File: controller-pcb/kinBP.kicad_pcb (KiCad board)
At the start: 2 copper layers, 100 x 86.5 mm, 30 parts, among them J1 LEFT_TOP, J10 LEFT_THUMB, J11 RIGHT_THUMB, J12 RIGHT_THUMB, J13 LEFT_THUMB, J2 LEFT_TOP, J3 RIGHT_TOP, J4 RIGHT_TOP, J5 RIGHT_KEYWELL, J6 LEFT_KEYWELL, J7 LEFT_THUMB, J8 RIGHT_THUMB, J9 Conn_02x08_Odd_Even, U1 weact_STM32F4x1

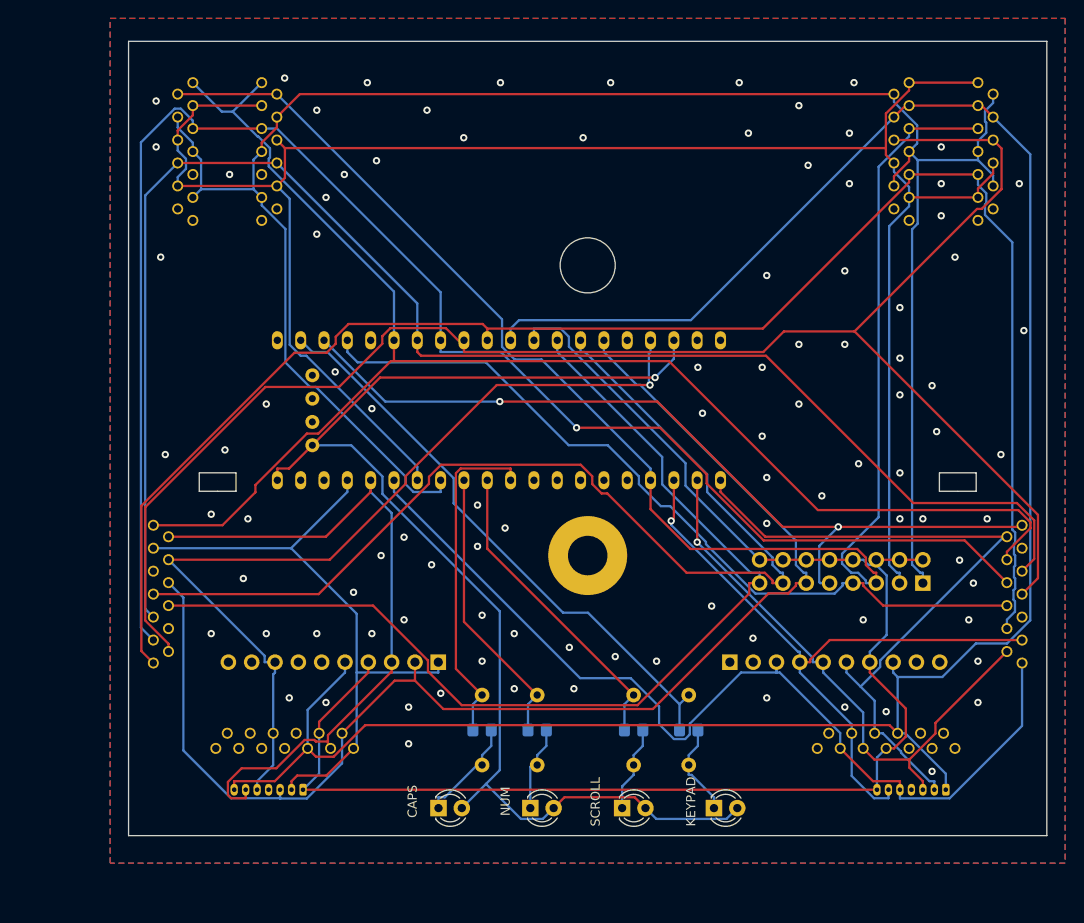
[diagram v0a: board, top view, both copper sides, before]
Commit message: River's modified version. Added piezo sounder. Rerouted. Split extra switch header.
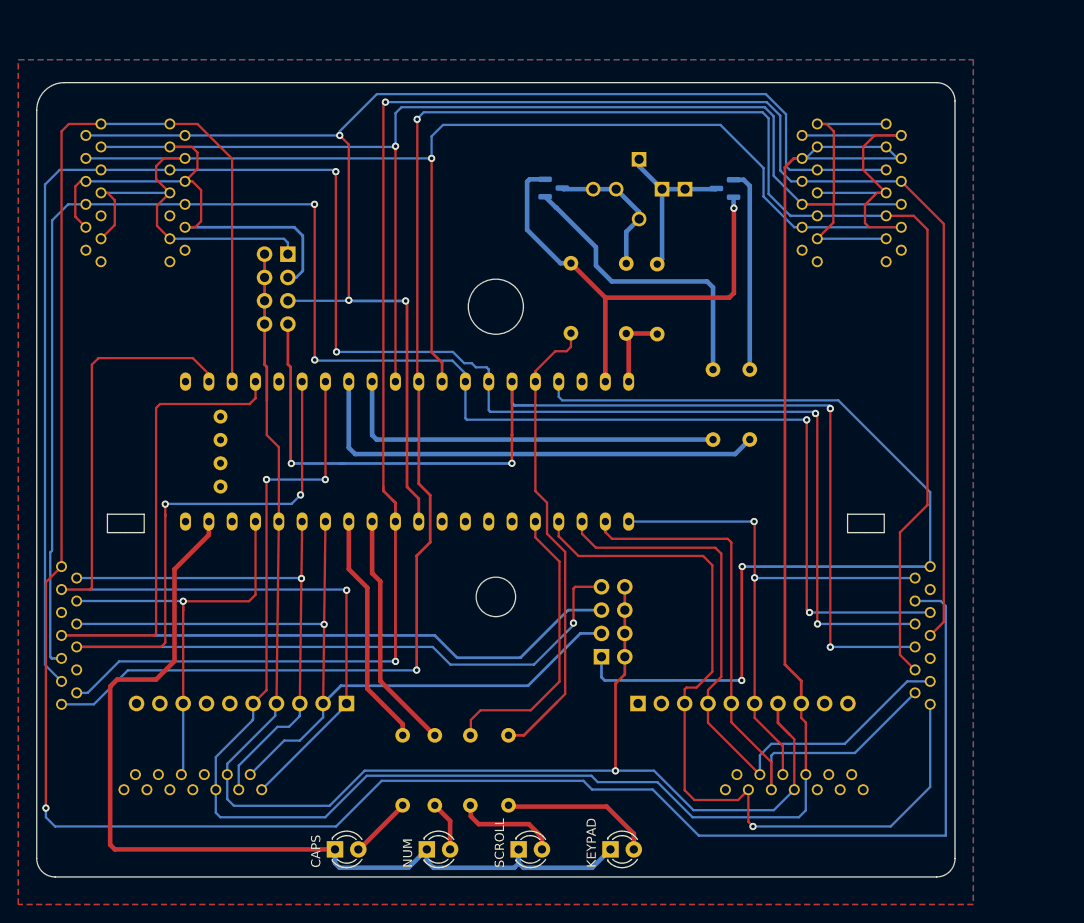
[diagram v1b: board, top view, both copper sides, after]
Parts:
- removed G***: LOGO, logo:qmk-small
- removed G1: LOGO, logo:q64logo
- removed J12: RIGHT_THUMB, Connector_Molex:Molex_PicoBlade_53048-0710_1x07_P1.25mm_Horizontal
- removed J13: LEFT_THUMB, Connector_Molex:Molex_PicoBlade_53048-0710_1x07_P1.25mm_Horizontal
- added J14: Conn_02x04_Odd_Even, Connector_PinHeader_2.54mm:PinHeader_2x04_P2.54mm_Vertical, B.Cu at (109.3, 73.7)
- added LS1: Speaker_Crystal, river:Piezos_12mm, B.Cu at (147.6, 66.6)
- added Q1: MMBT3904, Package_TO_SOT_SMD:SOT-23, B.Cu at (156.9, 66.5)
- added Q2: MMBT3904, Package_TO_SOT_SMD:SOT-23, B.Cu at (138.3, 66.5)
- added R9: R, Resistor_THT:R_Axial_DIN0207_L6.3mm_D2.5mm_P7.62mm_Horizontal, B.Cu at (146.2, 74.7)
- H1: value mounting pad -> hole; footprint MountingHole:MountingHole_4.3mm_M4_Pad -> MountingHole:MountingHole_4.3mm_M4
- H2: value mounting pad -> hole
- J9: value Conn_02x08_Odd_Even -> Conn_02x04_Odd_Even; footprint Connector_PinHeader_2.54mm:PinHeader_2x08_P2.54mm_Vertical -> Connector_PinHeader_2.54mm:PinHeader_2x04_P2.54mm_Vertical
- LED1, LED2, LED3, LED4: footprint LED_THT:LED_D3.0mm -> keyboards:LED_D3.0mm_centered
- R1: value 1k -> 100k; footprint Resistor_SMD:R_0805_2012Metric_Pad1.20x1.40mm_HandSolder -> Resistor_THT:R_Axial_DIN0207_L6.3mm_D2.5mm_P7.62mm_Horizontal
- R2, R3, R4: value 1k -> R; footprint Resistor_SMD:R_0805_2012Metric_Pad1.20x1.40mm_HandSolder -> Resistor_THT:R_Axial_DIN0207_L6.3mm_D2.5mm_P7.62mm_Horizontal
- moved R4 54.2 mm to (149.6, 74.8), turned to -90 degrees
- moved R1 45.1 mm to (140.2, 82.3), turned to 90 degrees
- moved R3 37.0 mm to (155.7, 93.9), turned to 90 degrees
- moved J9 35.9 mm to (143.5, 117.5), turned to 0 degrees
- moved R2 34.1 mm to (159.7, 93.9), turned to 90 degrees
- moved R5 23.0 mm to (133.4, 133.7), turned to 90 degrees
- moved R6 21.5 mm to (129.2, 133.7), turned to 90 degrees
- moved R7 16.4 mm to (125.3, 133.7), turned to 90 degrees
- moved R8 14.8 mm to (121.8, 133.7), turned to 90 degrees
- moved H1 11.0 mm to (132.0, 111.0)
- moved H2 11.0 mm to (132.0, 79.4)
- moved J1 11.0 mm to (96.5, 67.0)
- moved J10 11.0 mm to (99.0, 132.0)
- moved J11 11.0 mm to (164.5, 132.0)
- moved J2 11.0 mm to (89.0, 67.0)
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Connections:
- J7 pad 9: unconnected-(J7-Pad9) -> GND
- J8 pad 9: unconnected-(J8-Pad9) -> GND
- J9 pad 1: ROW_E -> ROW_A
- J9 pad 3: ROW_D -> ROW_2
- J9 pad 5: ROW_C -> ROW_1
- J9 pad 7: ROW_B -> ROW_0
- LED1 pad 1: LED_KPD_R -> GND
- LED1 pad 2: /3V3 -> Net-(LED1-A)
- LED2 pad 1: LED_SCRL_R -> GND
- LED2 pad 2: /3V3 -> Net-(LED2-A)
- LED3 pad 1: LED_NUM_R -> GND
- LED3 pad 2: /3V3 -> Net-(LED3-A)
- LED4 pad 1: LED_CAPS_R -> GND
- LED4 pad 2: /3V3 -> Net-(LED4-A)
- R1 pad 2: LED_KPD_R -> GND
- R2 pad 1: LED_SCRL -> PIEZO_A
- R2 pad 2: LED_SCRL_R -> Net-(Q1-B)
- R3 pad 1: LED_NUM -> PIEZO_B
- R3 pad 2: LED_NUM_R -> Net-(Q2-B)
- R4 pad 1: LED_CAPS -> Net-(Q1-C)
- R4 pad 2: LED_CAPS_R -> +5V
- R5 pad 1: LED_KPD -> Net-(LED1-A)
- R5 pad 2: LED_KPD_R -> LED_KPD
- R6 pad 1: LED_SCRL -> Net-(LED2-A)
- R6 pad 2: LED_SCRL_R -> LED_SCRL
- R7 pad 1: LED_NUM -> Net-(LED3-A)
- R7 pad 2: LED_NUM_R -> LED_NUM
- R8 pad 1: LED_CAPS -> Net-(LED4-A)
- R8 pad 2: LED_CAPS_R -> LED_CAPS
- U1 pad 10: LED_CAPS -> ROW_C
- U1 pad 11: LED_SCRL -> COL_3
- U1 pad 13: ROW_E -> LED_CAPS
- U1 pad 14: ROW_D -> ROW_2
- U1 pad 15: ROW_6 -> ROW_5
- U1 pad 16: ROW_5 -> COL_6
- U1 pad 17: ROW_4 -> ROW_3
- U1 pad 20: /3V3 -> +3V3
- U1 pad 22: LED_KPD -> ROW_4
- U1 pad 23: ROW_A -> COL_0
- U1 pad 24: ROW_B -> ROW_1
- U1 pad 26: COL_0 -> ROW_0
- U1 pad 27: COL_1 -> COL_5
- U1 pad 28: COL_2 -> PIEZO_A
- U1 pad 29: COL_3 -> PIEZO_B
- U1 pad 30: COL_4 -> ROW_D
- U1 pad 31: COL_5 -> COL_4
- U1 pad 32: COL_6 -> ROW_E
- U1 pad 33: ROW_0 -> COL_1
- U1 pad 34: ROW_1 -> COL_2
- U1 pad 35: ROW_2 -> ROW_B
- U1 pad 36: unconnected-(U1-Pad36) -> LED_KPD
- U1 pad 37: ROW_3 -> ROW_A
- U1 pad 38: /3V3 -> unconnected-(U1-3V3-Pad38)
- U1 pad 4: ROW_C -> ROW_6
- U1 pad 40: unconnected-(U1-Pad40) -> +5V
- U1 pad 41: /3V3 -> unconnected-(U1-3V3-Pad41)
- U1 pad 44: GND -> unconnected-(U1-GND-Pad44)
- U1 pad 5: unconnected-(U1-Pad5) -> LED_SCRL
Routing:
- net GND: track 0.00 -> 157.9 mm, vias 97 -> 1
- net /3V3: track 135.0 -> 0.00 mm, vias 1 -> 0
- net COL_0: track 160.5 -> 251.7 mm, vias 0 -> 1
- net PIEZO_A: track 0.00 -> 51.8 mm
- net ROW_3: track 97.1 -> 46.9 mm
- net ROW_2: track 142.2 -> 92.3 mm, vias 0 -> 1
- net PIEZO_B: track 0.00 -> 43.1 mm
- net COL_4: track 178.3 -> 217.0 mm, vias 0 -> 2
- net ROW_B: track 86.5 -> 120.7 mm, vias 0 -> 4
- net Net-(Q2-B): track 0.00 -> 32.5 mm
- net COL_3: track 182.1 -> 213.3 mm, vias 0 -> 2
- net ROW_4: track 69.0 -> 97.9 mm, vias 0 -> 1
- net COL_5: track 242.5 -> 219.2 mm, vias 0 -> 2
- net Net-(Q1-B): track 0.00 -> 22.0 mm
- net COL_2: track 176.9 -> 198.2 mm, vias 1 -> 4
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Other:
- outline, holes or cut-outs redrawn
- board text added: "Kinesis Black Pill V0.1 https://river.cat/t/kinbp"
- board text removed: "Col 6"
- board text removed: "KinBP v1.21"
- board text removed: "Open Hardware: CC-BY-SA"
- board text removed: "Rows E D C B A 2 1 0"
- board text removed: "github.com/DmNosachev/kinbp"
- board text removed: "pads"
- board text removed: "↑"

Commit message: V0.1 as manufactured
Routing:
- net ROW_6: track 88.2 -> 78.3 mm
- net ROW_7: track 68.4 -> 60.4 mm
- net ROW_8: track 66.3 -> 60.0 mm
- net COL_0: track 251.7 -> 245.9 mm
- net ROW_E: track 202.5 -> 198.8 mm
- net COL_5: track 219.2 -> 216.6 mm
- net ROW_D: track 207.9 -> 205.3 mm
- net COL_4: track 217.0 -> 214.9 mm
- net GND: track 157.9 -> 155.8 mm, vias 1 -> 220
- net COL_6: track 159.0 -> 156.9 mm
- net LED_KPD: track 51.0 -> 48.9 mm
- net LED_SCRL: track 31.6 -> 29.7 mm
- net COL_1: track 188.3 -> 186.9 mm
- net ROW_1: track 110.0 -> 109.0 mm
- net ROW_0: track 116.5 -> 115.5 mm
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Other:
- rule pad_to_mask_clearance: 0.0508 -> 0
- board text added: "JLCJLCJLCJLC"

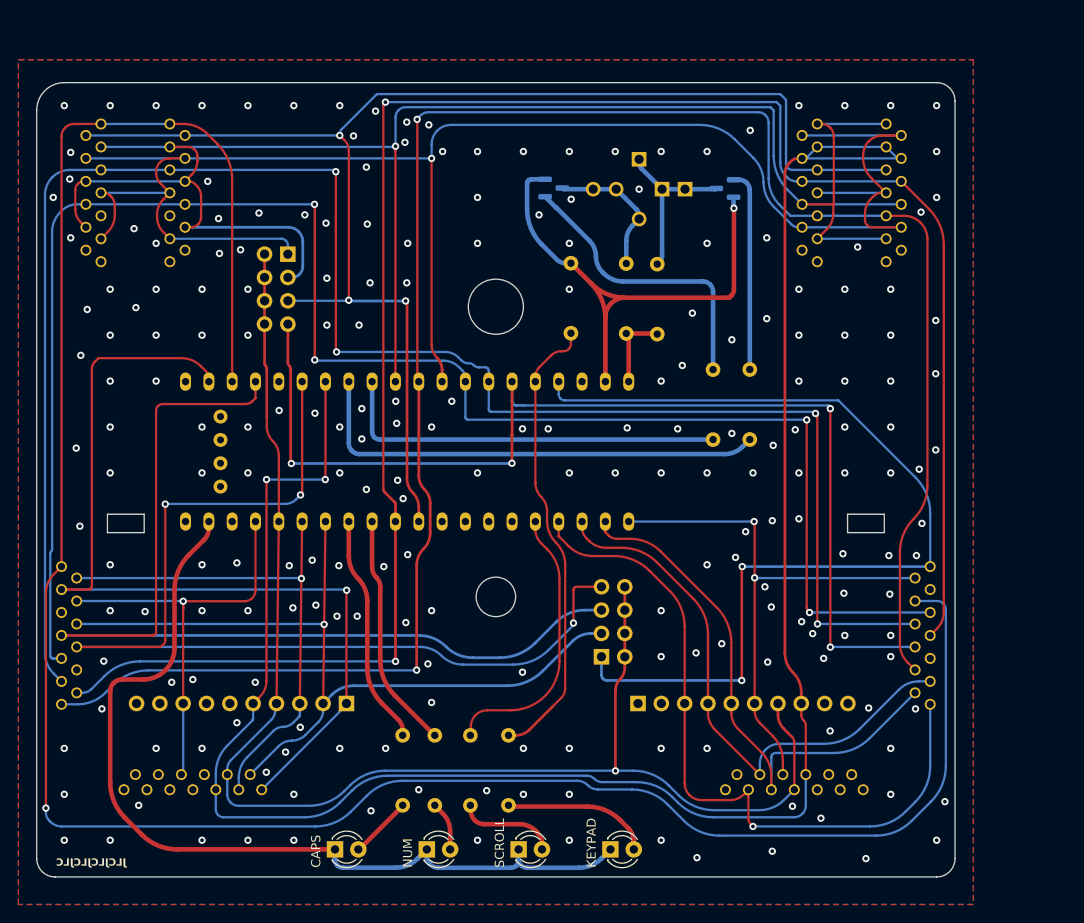
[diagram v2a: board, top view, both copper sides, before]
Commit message: Added connector for original external USB / footpedal cable. Fixed LED positions. Prob other stuff I forgot.
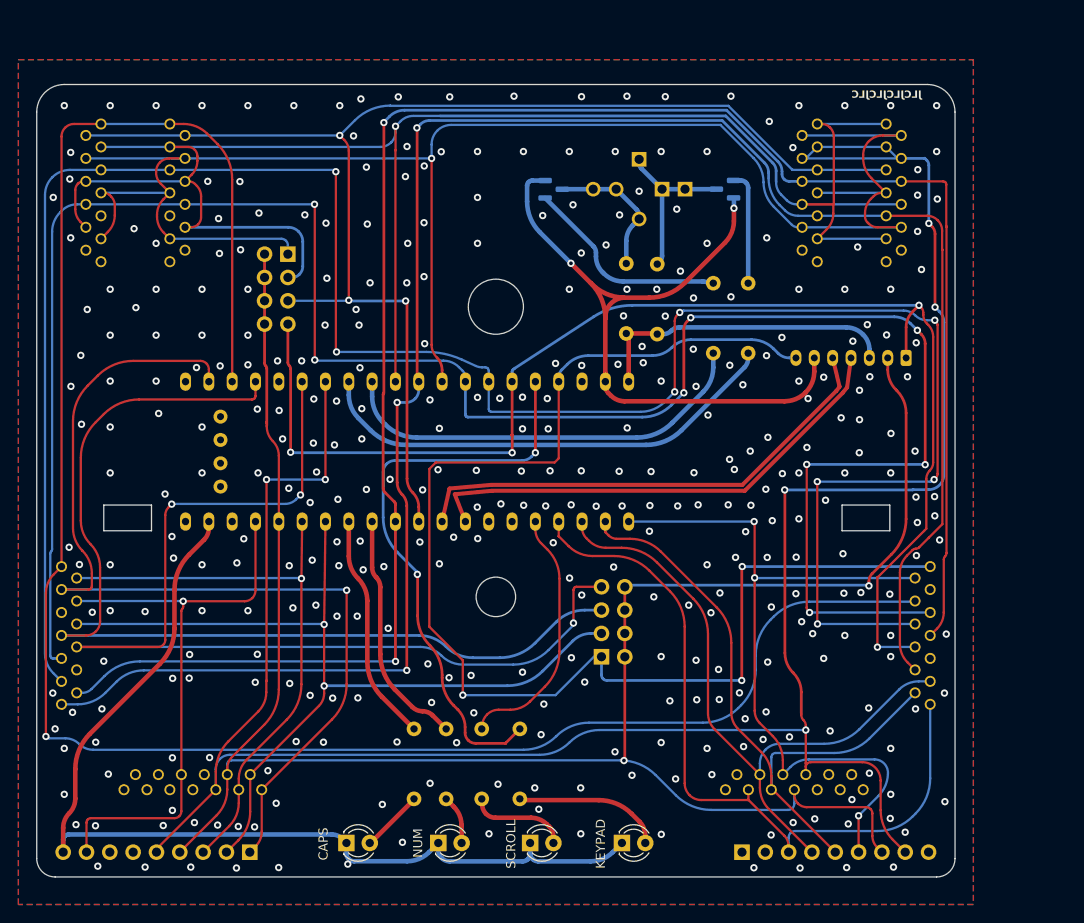
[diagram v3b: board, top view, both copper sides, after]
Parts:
- removed R1: 100k, Resistor_THT:R_Axial_DIN0207_L6.3mm_D2.5mm_P7.62mm_Horizontal
- added J15: USB Cable Socket, Connector_JST:JST_PH_B7B-PH-K_1x07_P2.00mm_Vertical, B.Cu at (176.7, 85.0)
- H1: footprint MountingHole:MountingHole_4.3mm_M4 -> river:MountingHole_4.3mm_M4_No_Copper
- J7, J8: footprint Connector_PinHeader_2.54mm:PinHeader_1x10_P2.54mm_Vertical -> Connector_PinHeader_2.54mm:PinHeader_1x09_P2.54mm_Vertical
- LS1: value Speaker_Crystal -> LD-BZEN-1205LOUDITY
- R4, R9: value R -> 470
- moved J8 19.8 mm to (158.8, 138.8)
- moved J7 19.3 mm to (105.2, 138.8)
- moved R3 9.41 mm to (155.7, 84.5)
- moved R2 9.40 mm to (159.5, 84.5)
- moved LED1 1.43 mm to (147.0, 137.8)
- moved LED2 1.43 mm to (137.0, 137.8)
- moved LED3 1.43 mm to (127.0, 137.8)
- moved LED4 1.43 mm to (117.0, 137.8)
- moved R5 1.42 mm to (134.6, 133.0)
- moved R6 1.42 mm to (130.5, 133.0)
- moved R7 1.42 mm to (126.6, 133.0)
- moved R8 1.42 mm to (123.1, 133.0)
- moved Q2 0.14 mm to (138.3, 66.6)
- moved Q1 0.07 mm to (156.9, 66.6)
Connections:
- U1 pad 8: unconnected-(U1-A11-Pad8) -> USB_D-
- U1 pad 9: unconnected-(U1-A12-Pad9) -> USB_D+
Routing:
- net COL_6: track 156.9 -> 223.0 mm, vias 1 -> 2
- net USB_D-: track 0.00 -> 53.9 mm
- net USB_D+: track 0.00 -> 53.9 mm
- net COL_2: track 197.4 -> 242.4 mm, vias 4 -> 8
- net COL_1: track 186.9 -> 231.4 mm, vias 4 -> 8
- net COL_5: track 216.6 -> 257.7 mm, vias 2 -> 6
- net ROW_A: track 104.5 -> 144.5 mm, vias 2 -> 3
- net GND: track 155.8 -> 188.2 mm, vias 220 -> 363
- net COL_0: track 245.9 -> 214.3 mm
- net +5V: track 8.28 -> 33.8 mm
- net ROW_B: track 120.4 -> 143.7 mm
- net ROW_9: track 59.7 -> 82.3 mm, vias 2 -> 3
- net ROW_3: track 46.6 -> 64.8 mm
- net LED_KPD: track 48.9 -> 63.6 mm, vias 0 -> 2
- net ROW_7: track 60.4 -> 71.0 mm
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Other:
- board size 100 x 86.5 mm -> 100 x 86.3 mm
- board text added: "5V"
- board text added: "COL_6"
- board text added: "Extra Switch Positions"
- board text added: "GND"
- board text added: "Kinesis External Connector"
- board text added: "ROW_A"
- board text added: "ROW_B"
- board text added: "USB D+"
- board text added: "USB D-"

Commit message: V0.2 as made, except then shifted screw hole down 0.2mm.
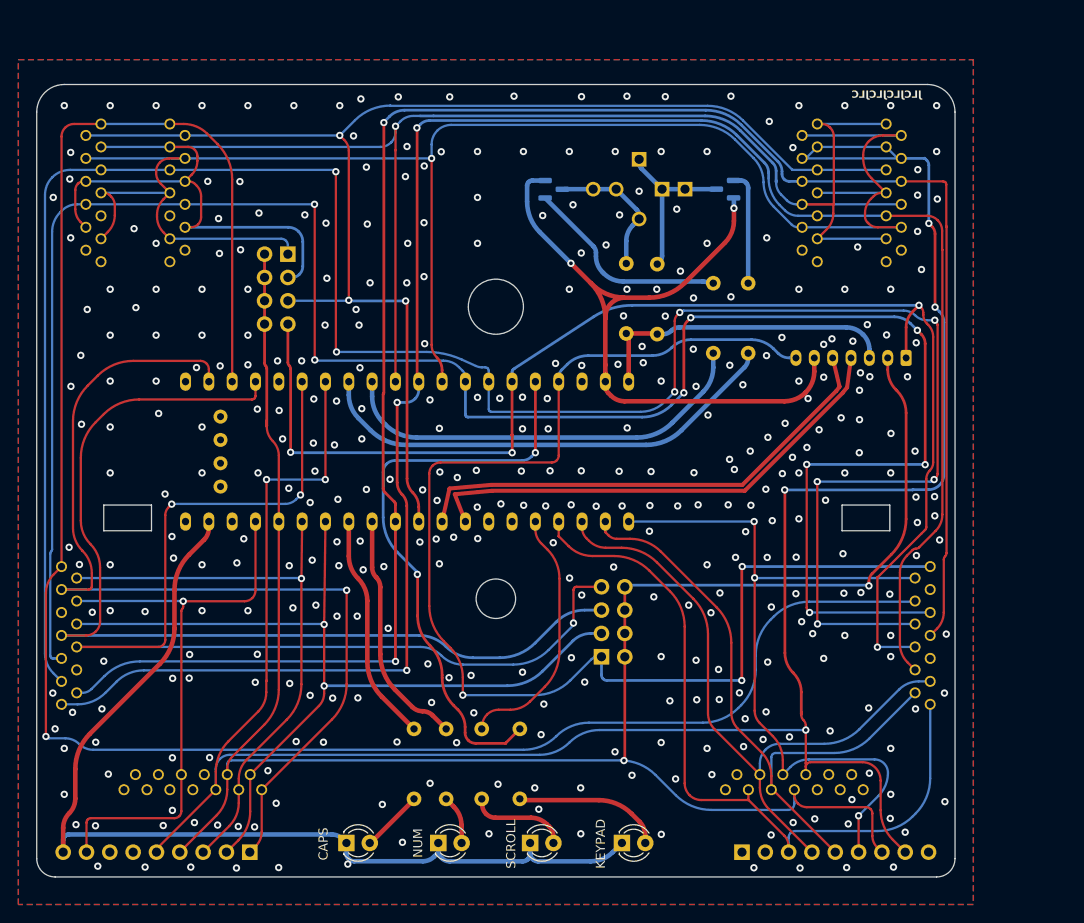
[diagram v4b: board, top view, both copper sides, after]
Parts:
- moved H1 0.20 mm to (132.0, 111.2)
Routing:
- net ROW_A: track 144.5 -> 143.1 mm
- net GND: track 188.2 -> 188.0 mm, vias 363 -> 372
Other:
- board text added: "Kinesis Black Pill V0.2 https://river.cat/t/kinbp"
- board text removed: "Kinesis Black Pill V0.1 https://river.cat/t/kinbp"

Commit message: Bumped version to V0.3. Added some notes, metadata.
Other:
- board text added: "Kinesis Black Pill V0.3 https://river.cat/t/kinbp"
- board text removed: "Kinesis Black Pill V0.2 https://river.cat/t/kinbp"
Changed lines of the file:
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@@
 	(paper "A4")
 	(title_block
-		(title "KinBP controller PCB")
-		(date "2022-06-20")
-		(rev "1.21")
+		(title "River's Blackpill Kinesis Controller")
+		(date "2024-07-08")
+		(rev "V0.3")
 	)
 	(layers
@@
 		)
 	)
-	(gr_text "Kinesis Black Pill V0.2\nhttps://river.cat/t/kinbp"
+	(gr_text "Kinesis Black Pill V0.3\nhttps://river.cat/t/kinbp"
 		(at 130.775 68.8 0)
 		(layer "B.SilkS")
